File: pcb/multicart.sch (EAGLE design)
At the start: 14 parts, among them IC1 74HCT373N, IC2 M27C4001B, Q1 BS170

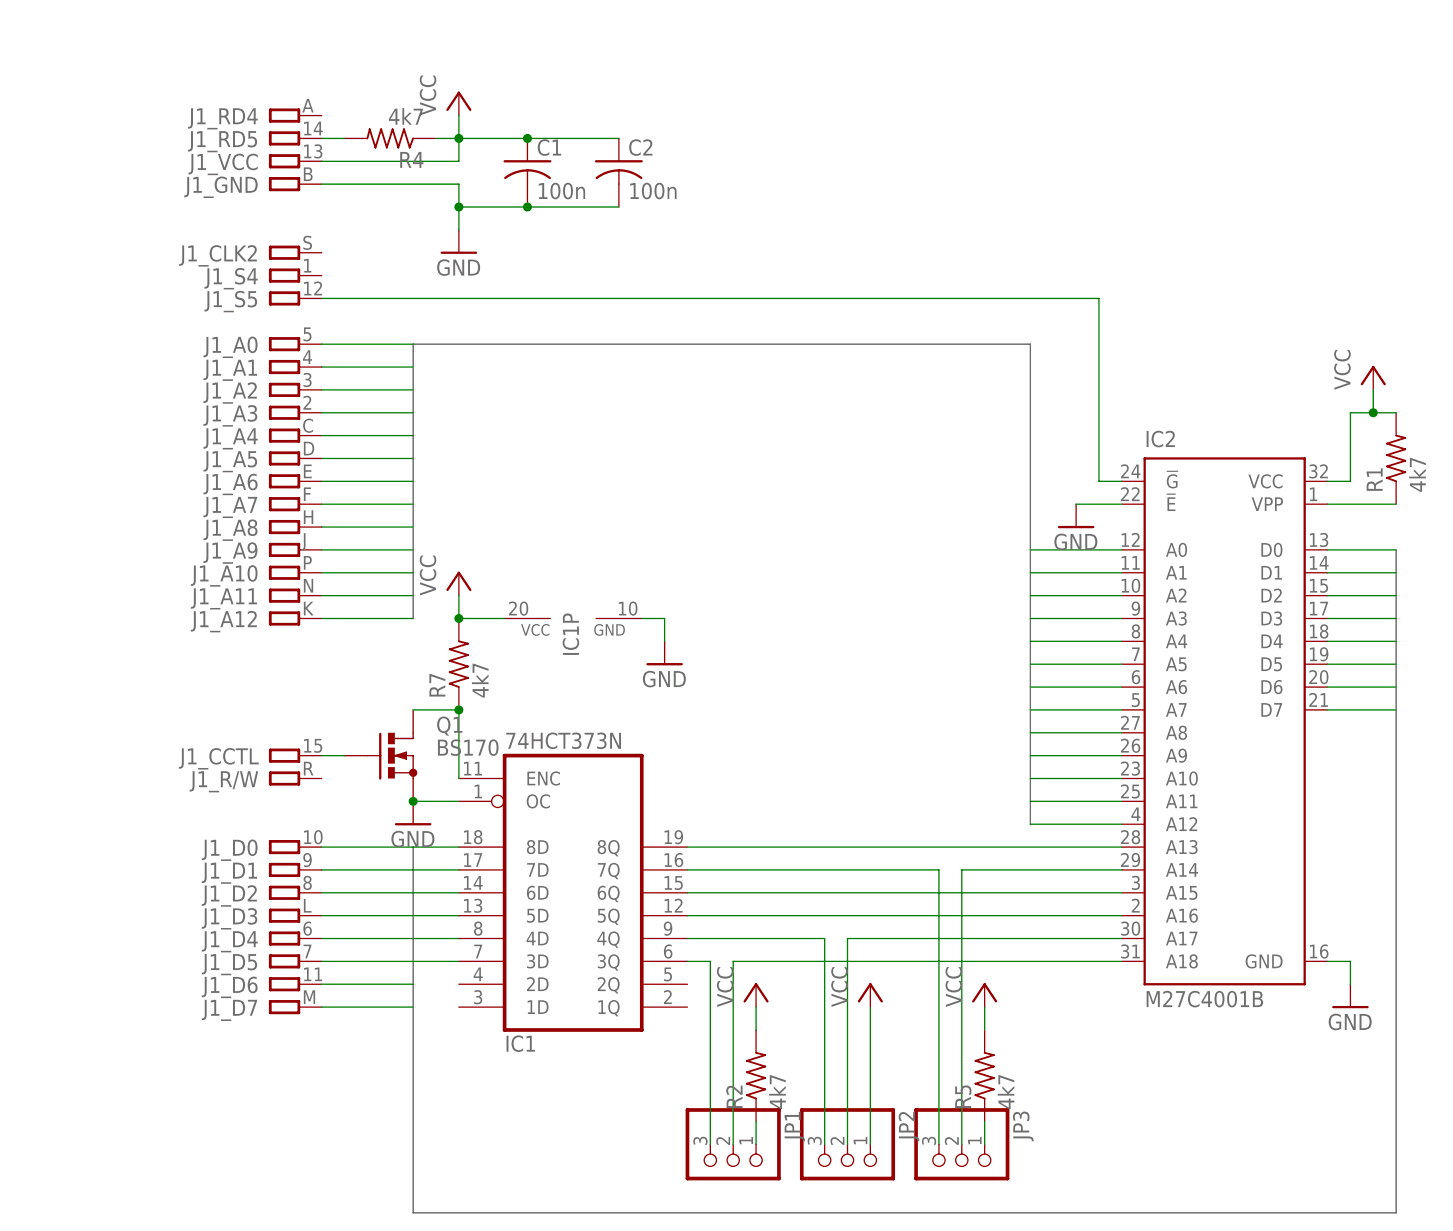
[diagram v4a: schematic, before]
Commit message: Modified the design to support both 8k and 16k standard games.
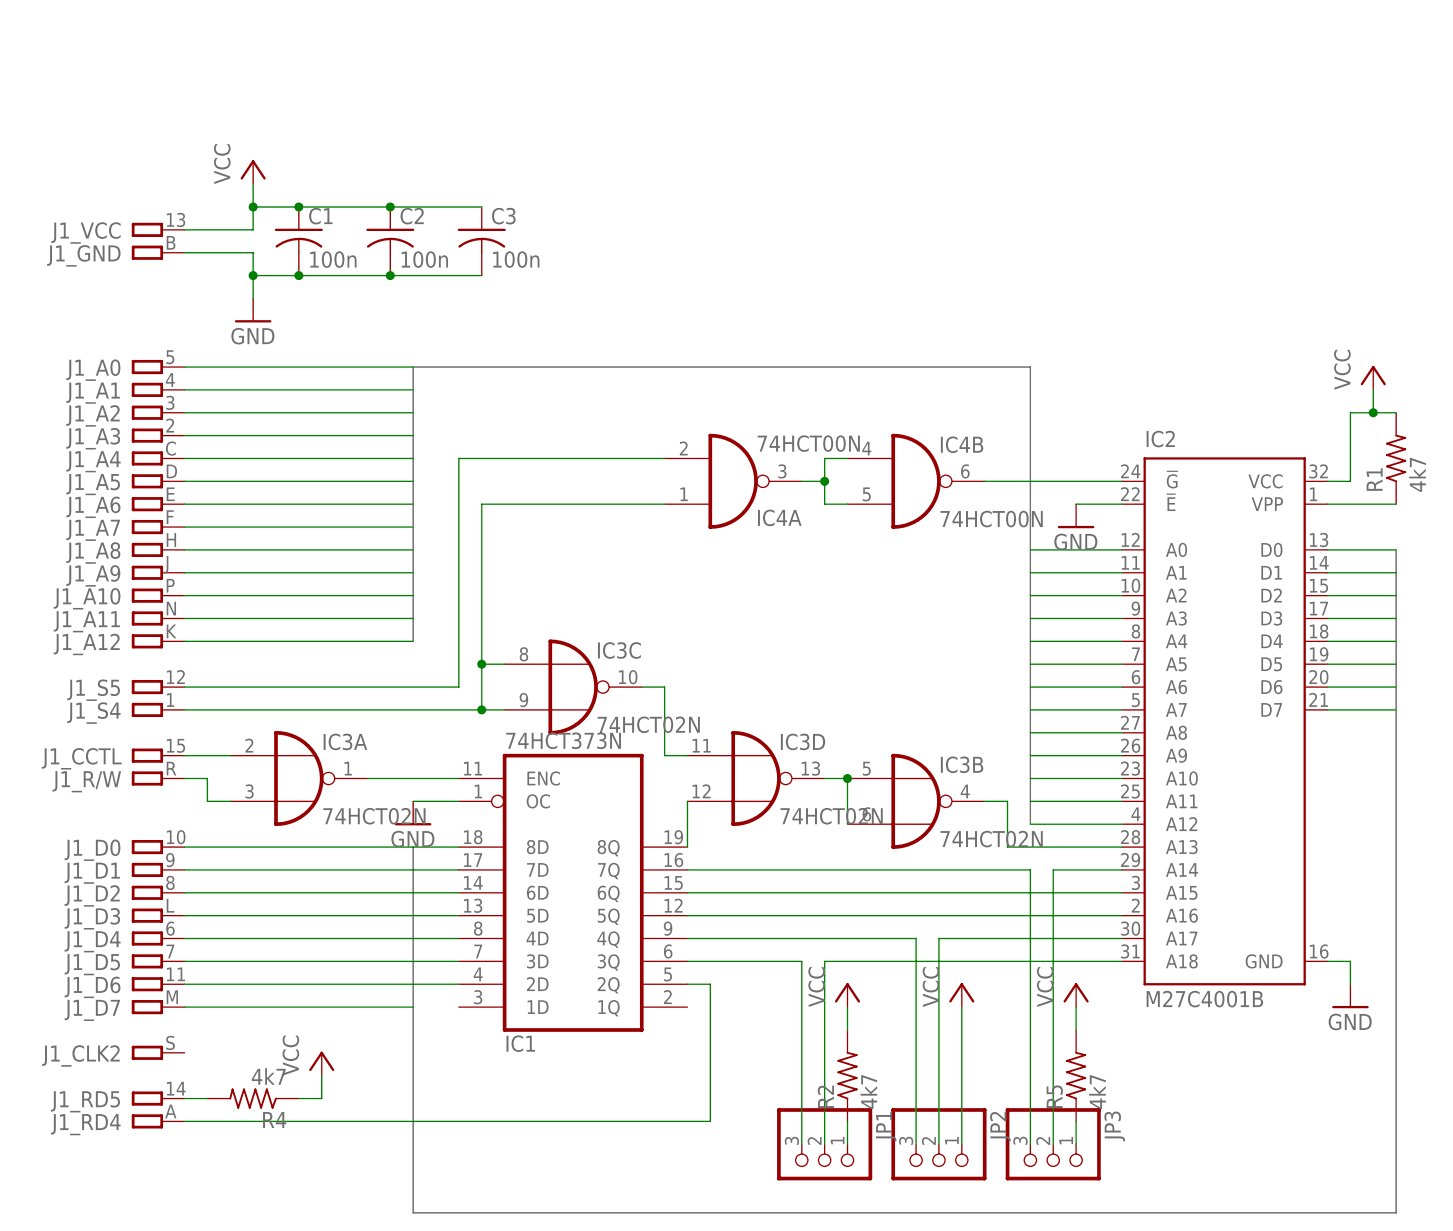
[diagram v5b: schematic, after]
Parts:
- removed Q1: BS170, transistor-small-signal:BS170
- removed R7: 4k7, resistor:R-US_0204/7
- added C3: 100n, resistor:C-US025-025X050
- added IC3: 74HCT02N, 74xx-eu:74HCT02N
- added IC4: 74HCT00N, 74xx-eu:74HCT00N
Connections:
- new net N$14: IC4A.O, IC4B.I0, IC4B.I1
- new net N$18: IC4A.I1, J1_S5.P
- new net N$19: IC3C.I0, IC3C.I1, IC4A.I0, J1_S4.P
- new net N$20: IC3A.I1, J1_R/W.P
- new net N$21: IC2.A13, IC3B.O
- new net N$22: IC1A.2Q, J1_RD4.P
- new net N$23: IC3B.I0, IC3B.I1, IC3D.O
- new net N$27: IC2.!G, IC4B.O
- net D6: now also IC1A.2D
- net GND: now also C3.2; no longer IC1P.GND, Q1.S
- net N$1: now also IC3D.I1; no longer IC2.A13
- net N$17: now also IC3C.O, IC3D.I0; no longer IC2.!G, J1_S5.P
- net N$7: now also IC3A.O; no longer Q1.D, R7.1
- net N$8: now also IC3A.I0; no longer Q1.G
- net VCC: now also C3.1; no longer IC1P.VCC, R7.2
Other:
- moved on the sheet: C1, C2, J1_A0, J1_A1, J1_A10, J1_A11, J1_A12, J1_A2, J1_A3, J1_A4, J1_A5, J1_A6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

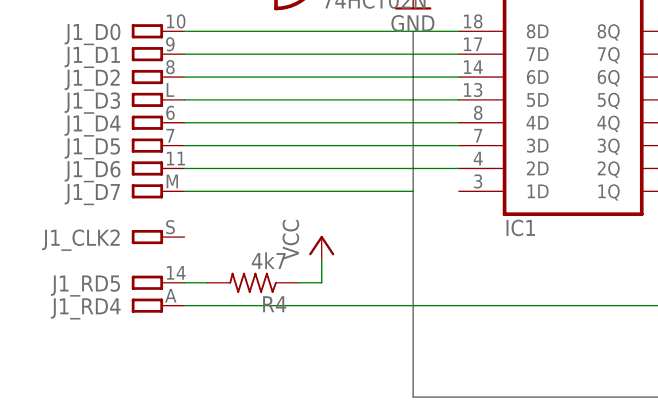
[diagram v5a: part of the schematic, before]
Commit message: Removed the RD5 line resistor.
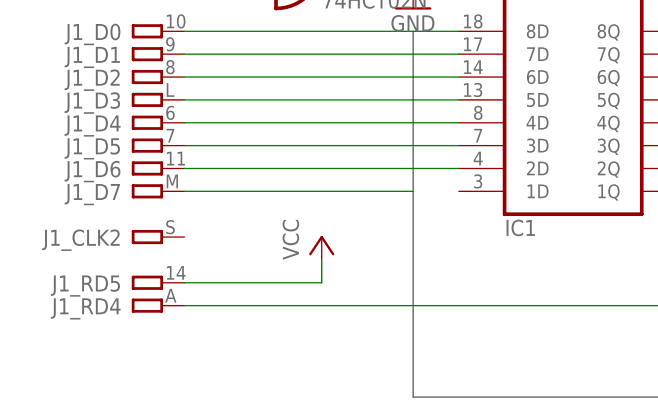
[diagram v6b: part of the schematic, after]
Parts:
- removed R4: 4k7, resistor:R-US_0204/7
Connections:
- removed net N$13: J1_RD5.P, R4.2
- net VCC: now also J1_RD5.P; no longer R4.1
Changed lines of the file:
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@@
 <part name="JP2" library="pinhead" deviceset="PINHD-1X3" device=""/>
 <part name="P+5" library="supply1" deviceset="VCC" device=""/>
-<part name="R4" library="resistor" deviceset="R-US_" device="0204/7" value="4k7"/>
 <part name="JP1" library="pinhead" deviceset="PINHD-1X3" device=""/>
 <part name="P+3" library="supply1" deviceset="VCC" device=""/>
@@
 <instance part="JP2" gate="A" x="81.28" y="12.7" rot="R270"/>
 <instance part="P+5" gate="VCC" x="83.82" y="33.02"/>
-<instance part="R4" gate="G$1" x="5.08" y="20.32" rot="R180"/>
 <instance part="JP1" gate="A" x="68.58" y="12.7" rot="R270"/>
 <instance part="P+3" gate="VCC" x="71.12" y="33.02"/>
@@
 <pinref part="P+4" gate="VCC" pin="VCC"/>
 <wire x1="12.7" y1="20.32" x2="12.7" y2="22.86" width="0.1524" layer="91"/>
-<pinref part="R4" gate="G$1" pin="1"/>
-<wire x1="10.16" y1="20.32" x2="12.7" y2="20.32" width="0.1524" layer="91"/>
+<pinref part="J1" gate="_RD5" pin="P"/>
+<wire x1="-2.54" y1="20.32" x2="12.7" y2="20.32" width="0.1524" layer="91"/>
 </segment>
 <segment>
@@
 </segment>
 </net>
-<net name="N$13" class="0">
-<segment>
-<pinref part="J1" gate="_RD5" pin="P"/>
-<wire x1="-2.54" y1="20.32" x2="0" y2="20.32" width="0.1524" layer="91"/>
-<pinref part="R4" gate="G$1" pin="2"/>
-</segment>
-</net>

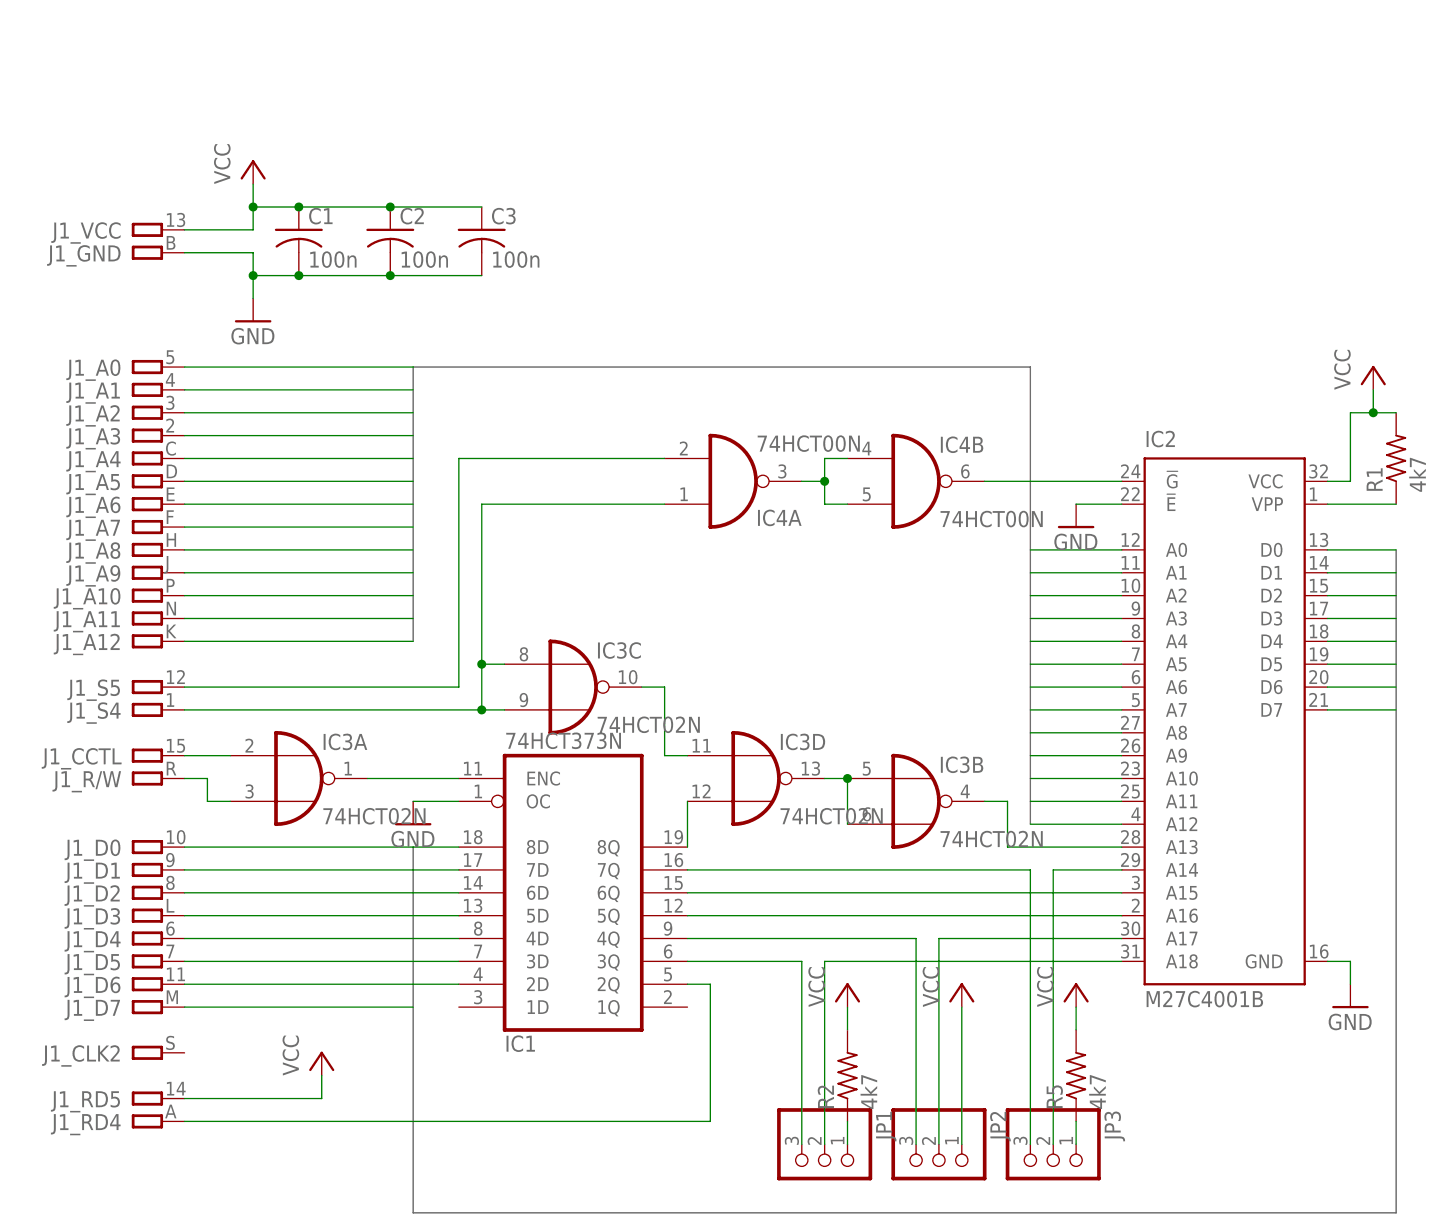
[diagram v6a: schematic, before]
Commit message: Added pull-downs to the CCTL & R/W lines.
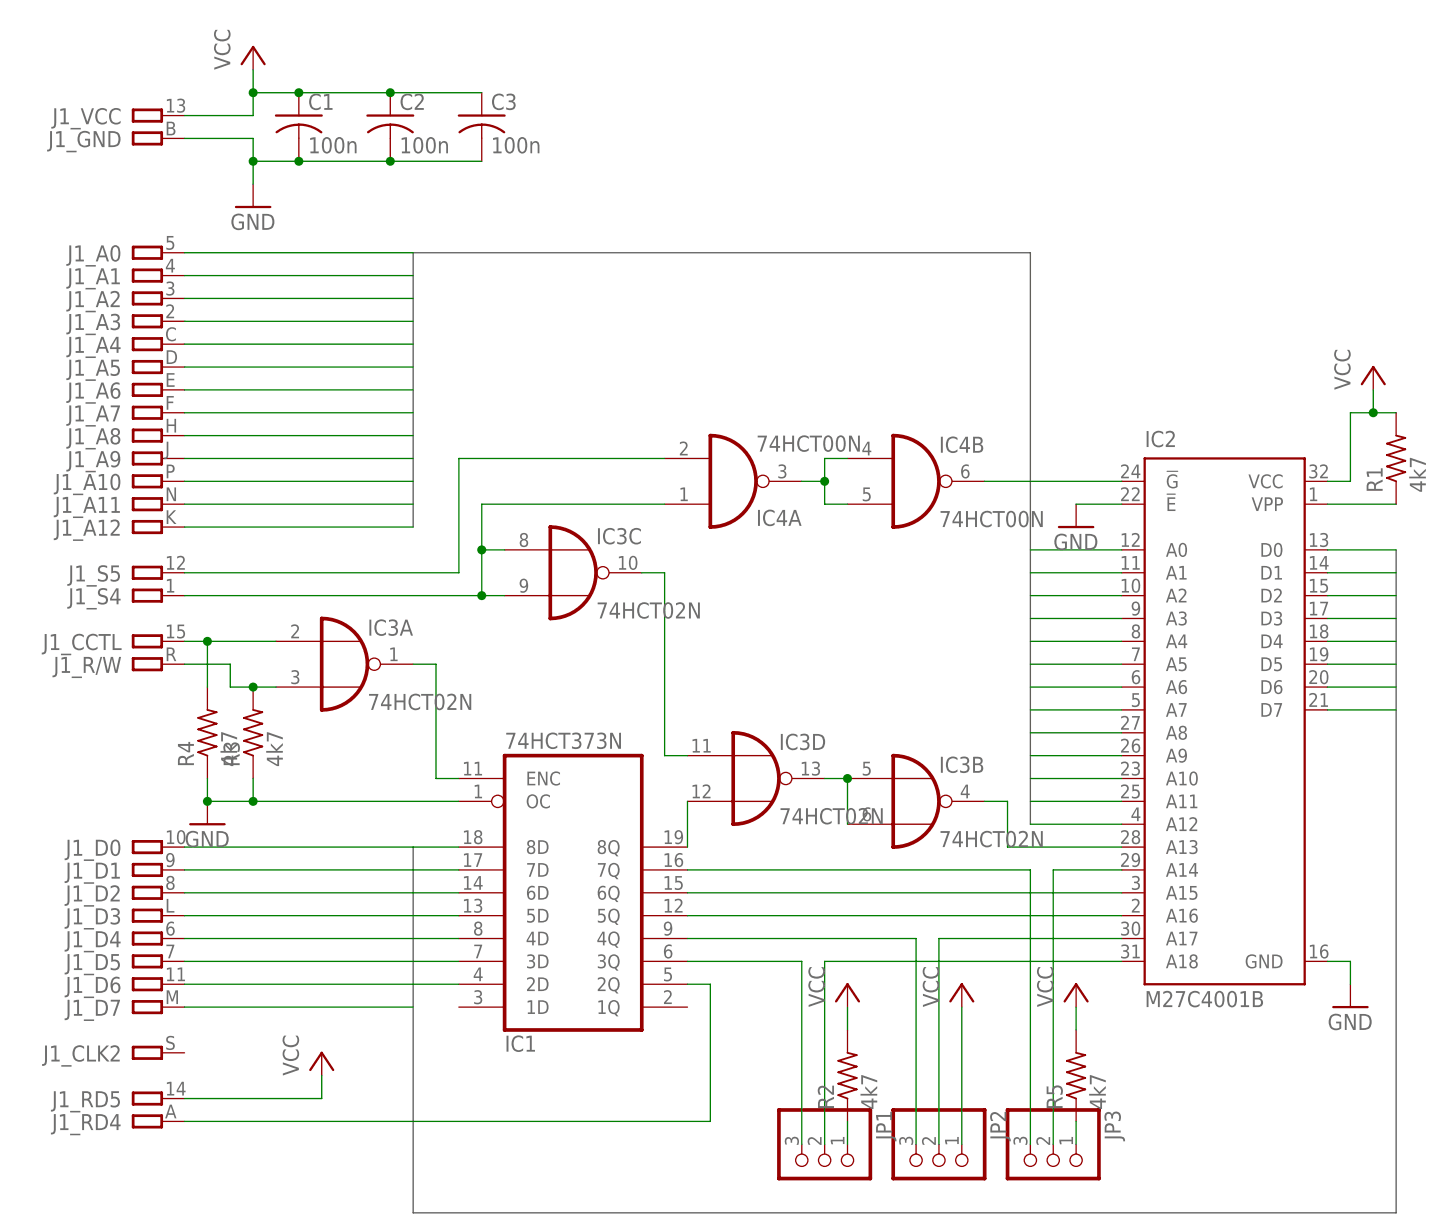
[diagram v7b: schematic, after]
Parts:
- added R3, R4: 4k7, resistor:R-US_0204/7
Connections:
- net GND: now also R3.1, R4.1
- net N$20: now also R3.2
- net N$8: now also R4.2
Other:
- moved on the sheet: C1, C2, C3, IC3A, IC3C, J1_A0, J1_A1, J1_A10, J1_A11, J1_A12, J1_A2, J1_A3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
